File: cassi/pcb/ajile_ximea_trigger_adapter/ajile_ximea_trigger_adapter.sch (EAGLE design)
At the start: 10 parts, among them K1 694108105102

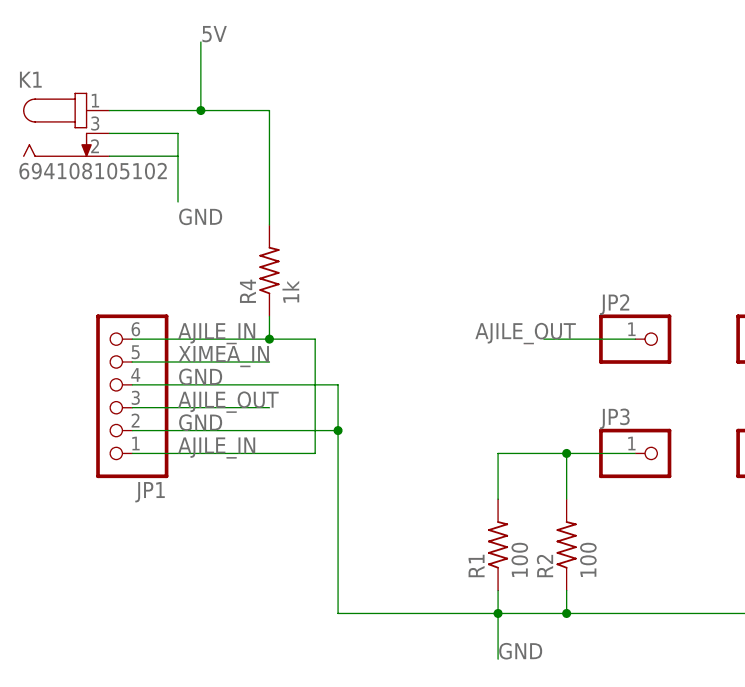
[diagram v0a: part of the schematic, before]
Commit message: put barrel jack on other side
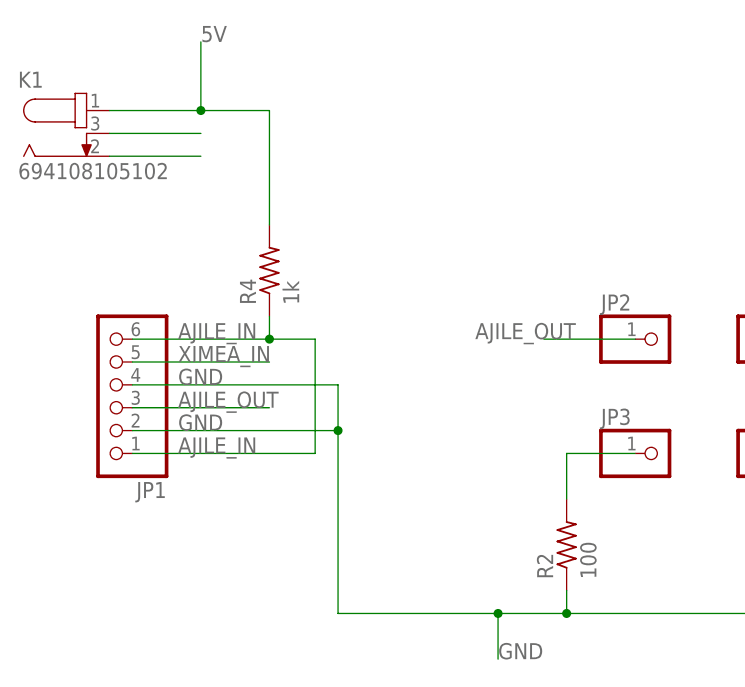
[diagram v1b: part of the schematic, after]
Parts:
- removed R1: 100, rcl:R-US_0204/7
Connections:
- new net N$1: K1.2
- new net N$3: K1.3
- net GND: no longer K1.2, K1.3, R1.1
- net N$2: no longer R1.2
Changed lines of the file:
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@@
 <part name="JP4" library="pinhead" library_urn="urn:adsk.eagle:library:325" deviceset="PINHD-1X1" device="" package3d_urn="urn:adsk.eagle:package:22485/2"/>
 <part name="JP5" library="pinhead" library_urn="urn:adsk.eagle:library:325" deviceset="PINHD-1X1" device="" package3d_urn="urn:adsk.eagle:package:22485/2"/>
-<part name="R1" library="rcl" library_urn="urn:adsk.eagle:library:334" deviceset="R-US_" device="0204/7" package3d_urn="urn:adsk.eagle:package:23498/1" value="100"/>
 <part name="R2" library="rcl" library_urn="urn:adsk.eagle:library:334" deviceset="R-US_" device="0204/7" package3d_urn="urn:adsk.eagle:package:23498/1" value="100"/>
 <part name="R3" library="rcl" library_urn="urn:adsk.eagle:library:334" deviceset="R-US_" device="0204/7" package3d_urn="urn:adsk.eagle:package:23498/1" value="2.2k"/>
@@
 <instance part="JP4" gate="G$1" x="76.2" y="45.72" rot="R180"/>
 <instance part="JP5" gate="G$1" x="76.2" y="33.02" rot="R180"/>
-<instance part="R1" gate="G$1" x="48.26" y="22.86" rot="R90"/>
 <instance part="R2" gate="G$1" x="55.88" y="22.86" rot="R90"/>
 <instance part="R3" gate="G$1" x="91.44" y="22.86" rot="R90"/>
@@
 <net name="GND" class="0">
 <segment>
-<pinref part="K1" gate="G$1" pin="2"/>
-<wire x1="5.08" y1="66.04" x2="12.7" y2="66.04" width="0.1524" layer="91"/>
-<pinref part="K1" gate="G$1" pin="3"/>
-<wire x1="5.08" y1="68.58" x2="12.7" y2="68.58" width="0.1524" layer="91"/>
-<wire x1="12.7" y1="68.58" x2="12.7" y2="60.96" width="0.1524" layer="91"/>
-<label x="12.7" y="58.42" size="1.778" layer="95"/>
-</segment>
-<segment>
 <pinref part="JP1" gate="A" pin="4"/>
 <wire x1="7.62" y1="40.64" x2="30.48" y2="40.64" width="0.1524" layer="91"/>
@@
 <label x="12.7" y="35.56" size="1.778" layer="95"/>
 <wire x1="30.48" y1="35.56" x2="30.48" y2="15.24" width="0.1524" layer="91"/>
-<pinref part="R1" gate="G$1" pin="1"/>
-<wire x1="48.26" y1="17.78" x2="48.26" y2="15.24" width="0.1524" layer="91"/>
 <wire x1="48.26" y1="15.24" x2="55.88" y2="15.24" width="0.1524" layer="91"/>
 <pinref part="R2" gate="G$1" pin="1"/>
@@
 <segment>
 <wire x1="63.5" y1="33.02" x2="55.88" y2="33.02" width="0.1524" layer="91"/>
-<pinref part="R1" gate="G$1" pin="2"/>
-<wire x1="55.88" y1="33.02" x2="48.26" y2="33.02" width="0.1524" layer="91"/>
-<wire x1="48.26" y1="33.02" x2="48.26" y2="27.94" width="0.1524" layer="91"/>
 <pinref part="R2" gate="G$1" pin="2"/>
 <wire x1="55.88" y1="27.94" x2="55.88" y2="33.02" width="0.1524" layer="91"/>
-<junction x="55.88" y="33.02"/>
 <pinref part="JP3" gate="G$1" pin="1"/>
 </segment>
 </net>
+<net name="N$1" class="0">
+<segment>
+<pinref part="K1" gate="G$1" pin="2"/>
+<wire x1="5.08" y1="66.04" x2="15.24" y2="66.04" width="0.1524" layer="91"/>
+</segment>
+</net>
+<net name="N$3" class="0">
+<segment>
+<pinref part="K1" gate="G$1" pin="3"/>
+<wire x1="5.08" y1="68.58" x2="15.24" y2="68.58" width="0.1524" layer="91"/>
+</segment>
+</net>

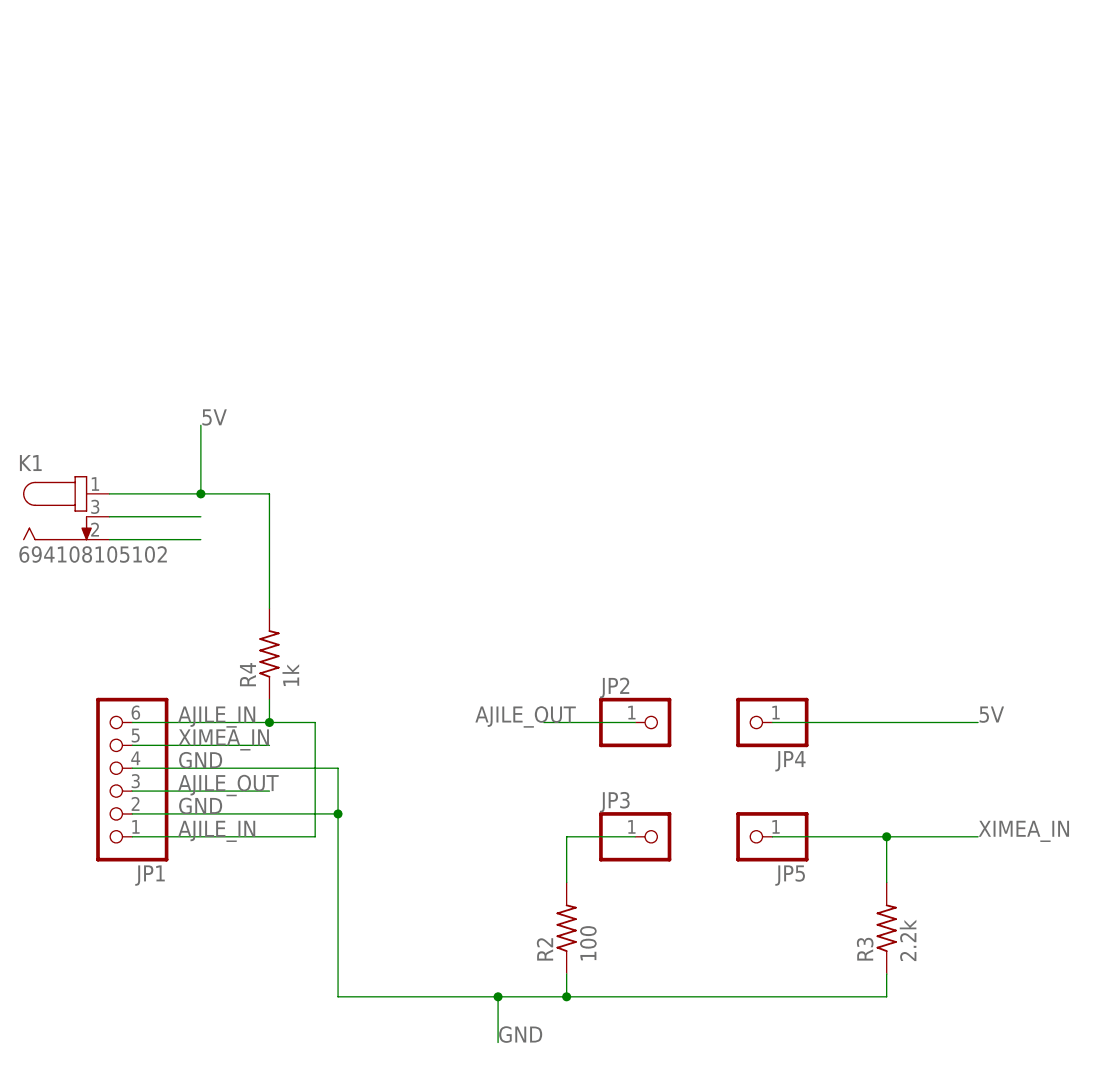
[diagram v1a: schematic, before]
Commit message: finished new ajile adapter pcb and added libraries used
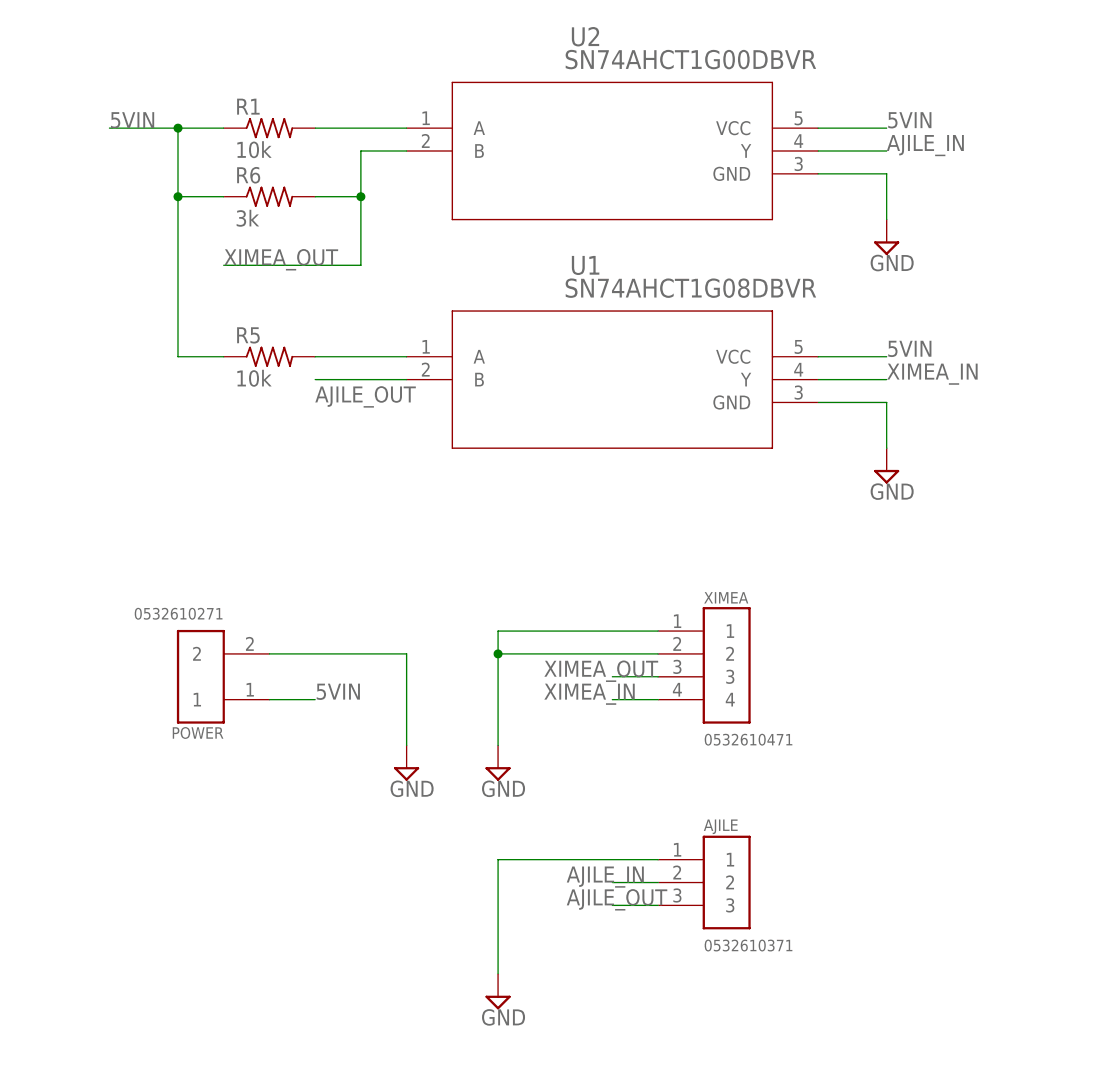
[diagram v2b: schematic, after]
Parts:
- removed JP1: (no value), pinhead:PINHD-1X6
- removed JP2, JP3, JP4, JP5: (no value), pinhead:PINHD-1X1
- removed K1: 694108105102, Wurth_Elektronik_Electromechanic_DC_Power_Jack_Connectors_rev15c:694108105102
- removed R2: 100, rcl:R-US_0204/7
- removed R3: 2.2k, rcl:R-US_0204/7
- removed R4: 1k, rcl:R-US_0204/7
- added AJILE: 0532610371, 0532610371:0532610371
- added POWER: 0532610271, 0532610271:0532610271
- added R1, R5: 10k, resistor:R-US_R0603
- added R6: 3k, resistor:R-US_R0603
- added U1: SN74AHCT1G08DBVR, sn74ahct:SN74AHCT1G08DBVR
- added U2: SN74AHCT1G00DBVR, sn74ahct1g00:SN74AHCT1G00DBVR
- added XIMEA: 0532610471, 0532610471:0532610471
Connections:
- removed net 5V: JP4.1, K1.1, R4.2
- removed net N$1: K1.2
- removed net N$2: JP3.1, R2.2
- removed net N$3: K1.3
- new net 5VIN: POWER.1, R1.1, R5.1, R6.1, U1.VCC, U2.VCC
- new net N$4: R1.2, U2.A
- new net N$6: R5.2, U1.A
- new net XIMEA_OUT: R6.2, U2.B, XIMEA.3
- net AJILE_IN: now also AJILE.2, U2.Y; no longer JP1.1, JP1.6, R4.1
- net AJILE_OUT: now also AJILE.3, U1.B; no longer JP1.3, JP2.1
- net GND: now also AJILE.1, POWER.2, U1.GND, U2.GND, XIMEA.1, XIMEA.2; no longer JP1.2, JP1.4, R2.1, R3.1
- net XIMEA_IN: now also U1.Y, XIMEA.4; no longer JP1.5, JP5.1, R3.2

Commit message: added final revisions to ximea trigger board
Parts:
- removed U1: SN74AHCT1G08DBVR, sn74ahct:SN74AHCT1G08DBVR
- added C1: 1uF, rcl:C-EUC0603
- added SN7408: SN74AHCT1G00DBVR, sn74ahct1g00:SN74AHCT1G00DBVR
- renumbered U2 to SN7400
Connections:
- removed net N$6: R5.2, U1.A
- new net N$1: R5.2, SN7408.A
- net 5VIN: now also C1.2, SN7408.VCC; no longer U1.VCC
- net AJILE_OUT: now also SN7408.B; no longer U1.B
- net GND: now also C1.1, SN7408.GND; no longer U1.GND
- net XIMEA_IN: now also SN7408.Y; no longer U1.Y
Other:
- moved on the sheet: POWER
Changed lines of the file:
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@@
 <?xml version="1.0" encoding="utf-8"?>
 <!DOCTYPE eagle SYSTEM "eagle.dtd">
-<eagle version="9.0.1">
+<eagle version="9.2.2">
 <drawing>
 <settings>
@@
 <part name="XIMEA" library="0532610471" deviceset="0532610471" device=""/>
 <part name="SUPPLY1" library="supply2" library_urn="urn:adsk.eagle:library:372" deviceset="GND" device=""/>
-<part name="U1" library="sn74ahct" deviceset="SN74AHCT1G08DBVR" device=""/>
 <part name="R1" library="resistor" library_urn="urn:adsk.eagle:library:348" deviceset="R-US_" device="R0603" package3d_urn="urn:adsk.eagle:package:26057/1" value="10k"/>
 <part name="R5" library="resistor" library_urn="urn:adsk.eagle:library:348" deviceset="R-US_" device="R0603" package3d_urn="urn:adsk.eagle:package:26057/1" value="10k"/>
@@
 <part name="SUPPLY5" library="supply2" library_urn="urn:adsk.eagle:library:372" deviceset="GND" device=""/>
 <part name="R6" library="resistor" library_urn="urn:adsk.eagle:library:348" deviceset="R-US_" device="R0603" package3d_urn="urn:adsk.eagle:package:26057/1" value="3k"/>
-<part name="U2" library="sn74ahct1g00" deviceset="SN74AHCT1G00DBVR" device=""/>
+<part name="SN7400" library="sn74ahct1g00" deviceset="SN74AHCT1G00DBVR" device=""/>
 <part name="AJILE" library="0532610371" deviceset="0532610371" device=""/>
+<part name="SN7408" library="sn74ahct1g00" deviceset="SN74AHCT1G00DBVR" device=""/>
+<part name="C1" library="rcl" library_urn="urn:adsk.eagle:library:334" deviceset="C-EU" device="C0603" package3d_urn="urn:adsk.eagle:package:23616/2" value="1uF"/>
 </parts>
 <sheets>
@@
 </plain>
 <instances>
-<instance part="POWER" gate="G$1" x="15.24" y="50.8" rot="R180"/>
-<instance part="XIMEA" gate="G$1" x="73.66" y="50.8"/>
-<instance part="SUPPLY1" gate="GND" x="38.1" y="40.64"/>
-<instance part="U1" gate="A" x="35.56" y="86.36"/>
-<instance part="R1" gate="G$1" x="22.86" y="111.76"/>
-<instance part="R5" gate="G$1" x="22.86" y="86.36"/>
-<instance part="SUPPLY2" gate="GND" x="91.44" y="73.66"/>
-<instance part="SUPPLY3" gate="GND" x="91.44" y="99.06"/>
-<instance part="SUPPLY4" gate="GND" x="48.26" y="40.64"/>
-<instance part="SUPPLY5" gate="GND" x="48.26" y="15.24"/>
-<instance part="R6" gate="G$1" x="22.86" y="104.14"/>
-<instance part="U2" gate="A" x="35.56" y="111.76"/>
-<instance part="AJILE" gate="G$1" x="73.66" y="27.94"/>
+<instance part="POWER" gate="G$1" x="10.16" y="50.8" smashed="yes" rot="R180">
+<attribute name="NAME" x="12.708659375" y="45.19295" size="1.27433125" layer="95" rot="R180"/>
+<attribute name="VALUE" x="12.70658125" y="58.439740625" size="1.273290625" layer="96" rot="R180"/>
+</instance>
+<instance part="XIMEA" gate="G$1" x="73.66" y="50.8" smashed="yes">
+<attribute name="NAME" x="71.11636875" y="58.9396" size="1.271809375" layer="95"/>
+<attribute name="VALUE" x="71.118159375" y="43.174490625" size="1.270909375" layer="96"/>
+</instance>
+<instance part="SUPPLY1" gate="GND" x="38.1" y="40.64" smashed="yes">
+<attribute name="VALUE" x="36.195" y="37.465" size="1.778" layer="96"/>
+</instance>
+<instance part="R1" gate="G$1" x="22.86" y="111.76" smashed="yes">
+<attribute name="NAME" x="19.05" y="113.2586" size="1.778" layer="95"/>
+<attribute name="VALUE" x="19.05" y="108.458" size="1.778" layer="96"/>
+</instance>
+<instance part="R5" gate="G$1" x="22.86" y="86.36" smashed="yes">
+<attribute name="NAME" x="19.05" y="87.8586" size="1.778" layer="95"/>
+<attribute name="VALUE" x="19.05" y="83.058" size="1.778" layer="96"/>
+</instance>
+<instance part="SUPPLY2" gate="GND" x="91.44" y="73.66" smashed="yes">
+<attribute name="VALUE" x="89.535" y="70.485" size="1.778" layer="96"/>
+</instance>
+<instance part="SUPPLY3" gate="GND" x="91.44" y="99.06" smashed="yes">
+<attribute name="VALUE" x="89.535" y="95.885" size="1.778" layer="96"/>
+</instance>
+<instance part="SUPPLY4" gate="GND" x="48.26" y="40.64" smashed="yes">
+<attribute name="VALUE" x="46.355" y="37.465" size="1.778" layer="96"/>
+</instance>
+<instance part="SUPPLY5" gate="GND" x="48.26" y="15.24" smashed="yes">
+<attribute name="VALUE" x="46.355" y="12.065" size="1.778" layer="96"/>
+</instance>
+<instance part="R6" gate="G$1" x="22.86" y="104.14" smashed="yes">
+<attribute name="NAME" x="19.05" y="105.6386" size="1.778" layer="95"/>
+<attribute name="VALUE" x="19.05" y="100.838" size="1.778" layer="96"/>
+</instance>
+<instance part="SN7400" gate="A" x="35.56" y="111.76" smashed="yes">
+<attribute name="NAME" x="56.2356" y="120.8786" size="2.0828" layer="95" ratio="6" rot="SR0"/>
+<attribute name="VALUE" x="55.6006" y="118.3386" size="2.0828" layer="96" ratio="6" rot="SR0"/>
+</instance>
+<instance part="AJILE" gate="G$1" x="73.66" y="27.94" smashed="yes">
+<attribute name="NAME" x="71.113140625" y="33.67043125" size="1.27343125" layer="95"/>
+<attribute name="VALUE" x="71.11455" y="20.30365" size="1.27273125" layer="96"/>
+</instance>
+<instance part="SN7408" gate="A" x="35.56" y="86.36" smashed="yes">
+<attribute name="NAME" x="56.2356" y="95.4786" size="2.0828" layer="95" ratio="6" rot="SR0"/>
+<attribute name="VALUE" x="55.6006" y="92.9386" size="2.0828" layer="96" ratio="6" rot="SR0"/>
+</instance>
+<instance part="C1" gate="G$1" x="30.48" y="48.26" smashed="yes" rot="R270">
+<attribute name="NAME" x="30.861" y="46.736" size="1.778" layer="95" rot="R270"/>
+<attribute name="VALUE" x="25.781" y="46.736" size="1.778" layer="96" rot="R270"/>
+</instance>
 </instances>
 <busses>
@@
 </segment>
 <segment>
-<pinref part="U1" gate="A" pin="Y"/>
 <wire x1="83.82" y1="83.82" x2="91.44" y2="83.82" width="0.1524" layer="91"/>
 <label x="91.44" y="83.82" size="1.778" layer="95"/>
+<pinref part="SN7408" gate="A" pin="Y"/>
 </segment>
 </net>
 <net name="AJILE_OUT" class="0">
 <segment>
-<pinref part="U1" gate="A" pin="B"/>
 <wire x1="38.1" y1="83.82" x2="27.94" y2="83.82" width="0.1524" layer="91"/>
 <label x="27.94" y="81.28" size="1.778" layer="95"/>
+<pinref part="SN7408" gate="A" pin="B"/>
 </segment>
 <segment>
@@
 <wire x1="83.82" y1="109.22" x2="91.44" y2="109.22" width="0.1524" layer="91"/>
 <label x="91.44" y="109.22" size="1.778" layer="95"/>
-<pinref part="U2" gate="A" pin="Y"/>
+<pinref part="SN7400" gate="A" pin="Y"/>
 </segment>
 <segment>
@@
 <pinref part="SUPPLY1" gate="GND" pin="GND"/>
 <pinref part="POWER" gate="G$1" pin="2"/>
-<wire x1="22.86" y1="53.34" x2="38.1" y2="53.34" width="0.1524" layer="91"/>
+<wire x1="17.78" y1="53.34" x2="38.1" y2="53.34" width="0.1524" layer="91"/>
 <wire x1="38.1" y1="53.34" x2="38.1" y2="43.18" width="0.1524" layer="91"/>
-</segment>
-<segment>
-<pinref part="U1" gate="A" pin="GND"/>
+<pinref part="C1" gate="G$1" pin="1"/>
+<wire x1="38.1" y1="53.34" x2="38.1" y2="48.26" width="0.1524" layer="91"/>
+<wire x1="38.1" y1="48.26" x2="33.02" y2="48.26" width="0.1524" layer="91"/>
+<junction x="38.1" y="53.34"/>
+</segment>
+<segment>
 <wire x1="83.82" y1="81.28" x2="91.44" y2="81.28" width="0.1524" layer="91"/>
 <wire x1="91.44" y1="81.28" x2="91.44" y2="76.2" width="0.1524" layer="91"/>
 <pinref part="SUPPLY2" gate="GND" pin="GND"/>
+<pinref part="SN7408" gate="A" pin="GND"/>
 </segment>
 <segment>
@@
 <wire x1="91.44" y1="106.68" x2="91.44" y2="101.6" width="0.1524" layer="91"/>
 <pinref part="SUPPLY3" gate="GND" pin="GND"/>
-<pinref part="U2" gate="A" pin="GND"/>
+<pinref part="SN7400" gate="A" pin="GND"/>
 </segment>
 <segment>
@@
 <wire x1="83.82" y1="111.76" x2="91.44" y2="111.76" width="0.1524" layer="91"/>
 <label x="91.44" y="111.76" size="1.778" layer="95"/>
-<pinref part="U2" gate="A" pin="VCC"/>
-</segment>
-<segment>
-<pinref part="U1" gate="A" pin="VCC"/>
+<pinref part="SN7400" gate="A" pin="VCC"/>
+</segment>
+<segment>
 <wire x1="83.82" y1="86.36" x2="91.44" y2="86.36" width="0.1524" layer="91"/>
 <label x="91.44" y="86.36" size="1.778" layer="95"/>
+<pinref part="SN7408" gate="A" pin="VCC"/>
 </segment>
 <segment>
@@
 <segment>
 <pinref part="POWER" gate="G$1" pin="1"/>
-<wire x1="22.86" y1="48.26" x2="27.94" y2="48.26" width="0.1524" layer="91"/>
-<label x="27.94" y="48.26" size="1.778" layer="95"/>
+<label x="17.78" y="48.26" size="1.778" layer="95"/>
+<pinref part="C1" gate="G$1" pin="2"/>
+<wire x1="17.78" y1="48.26" x2="25.4" y2="48.26" width="0.1524" layer="91"/>
 </segment>
 </net>
@@
 <junction x="33.02" y="104.14"/>
 <label x="17.78" y="96.52" size="1.778" layer="95"/>
-<pinref part="U2" gate="A" pin="B"/>
+<pinref part="SN7400" gate="A" pin="B"/>
 </segment>
 </net>
@@
 <wire x1="38.1" y1="111.76" x2="27.94" y2="111.76" width="0.1524" layer="91"/>
 <pinref part="R1" gate="G$1" pin="2"/>
-<pinref part="U2" gate="A" pin="A"/>
-</segment>
-</net>
-<net name="N$6" class="0">
-<segment>
-<pinref part="U1" gate="A" pin="A"/>
-<wire x1="38.1" y1="86.36" x2="27.94" y2="86.36" width="0.1524" layer="91"/>
+<pinref part="SN7400" gate="A" pin="A"/>
+</segment>
+</net>
+<net name="N$1" class="0">
+<segment>
 <pinref part="R5" gate="G$1" pin="2"/>
+<pinref part="SN7408" gate="A" pin="A"/>
+<wire x1="27.94" y1="86.36" x2="38.1" y2="86.36" width="0.1524" layer="91"/>
 </segment>
 </net>
@@
 packages will not be understood (or retained) with this version.
 </note>
+<note version="8.4" severity="warning">
+Since Version 8.4, EAGLE supports properties for SPICE simulation.
+Probes in schematics and SPICE mapping objects found in parts and library devices
+will not be understood with this version. Update EAGLE to the latest version
+for full support of SPICE simulation.
+</note>
 </compatibility>
